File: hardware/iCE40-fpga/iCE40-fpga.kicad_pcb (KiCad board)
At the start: 4 copper layers, 50 x 22.9 mm, 66 parts, among them J1 USB_B_Micro, J2 JST_PH, J3 Feather, Q1 DMP2045U, U1 MCP73831-2-OT, U2 W25Q32JVZP, U3 AP2112K-3.3, U5 AP2112K-1.2, U6 ICE40UP5K-SG48ITR, U7 93C46B, U8 FT2232H, X1 DSC6101CI1A

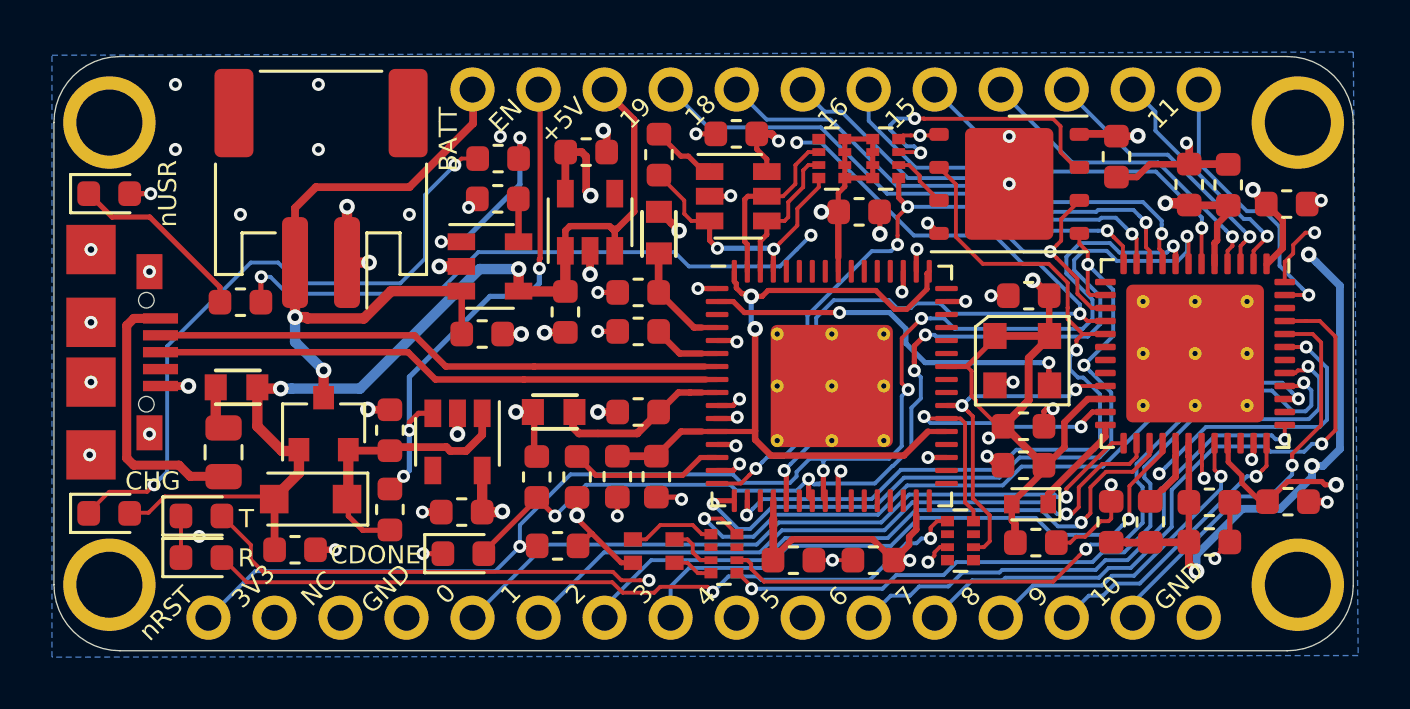
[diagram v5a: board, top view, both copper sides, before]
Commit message: changes to make everything work with new library setup
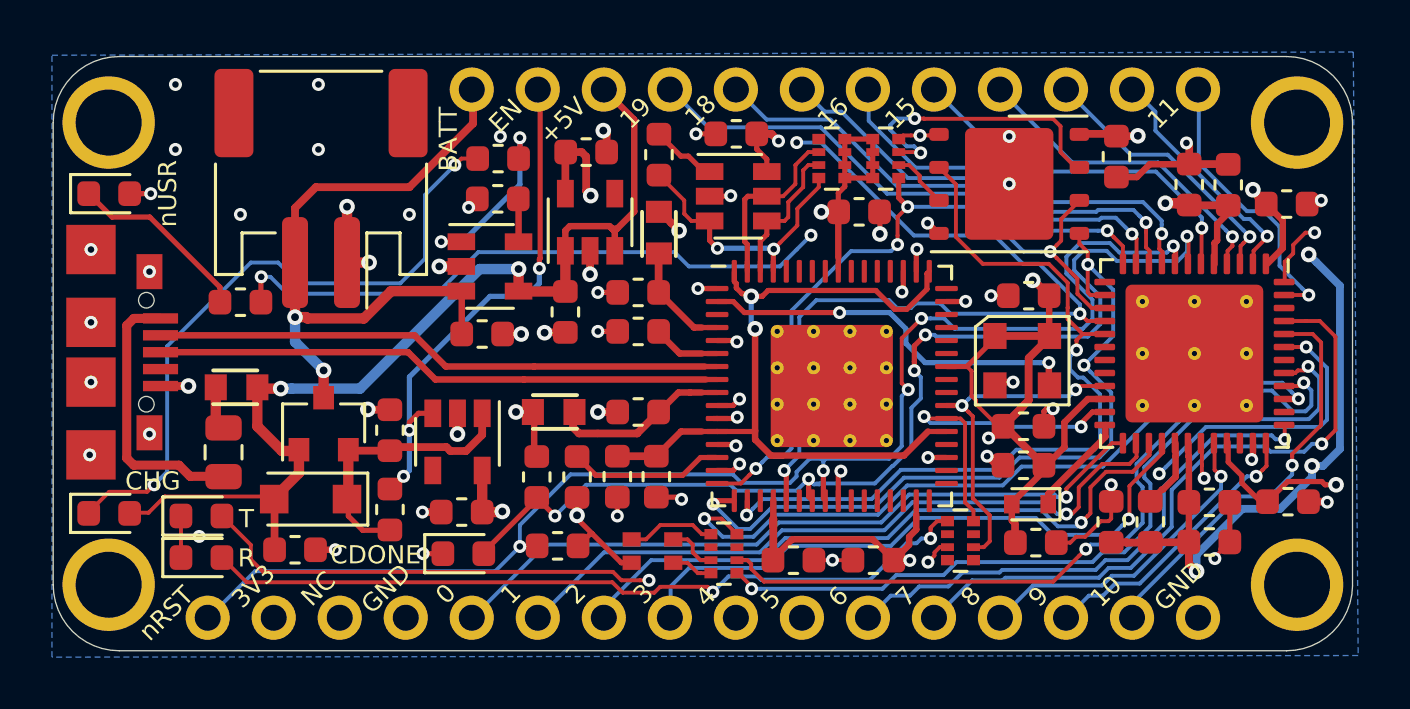
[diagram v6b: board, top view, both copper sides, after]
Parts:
- removed the REF** at (33.3, 38.6)
- removed the REF** at (66.7, 40.1)
- removed U8: FT2232H, josh-footprints:QFN-64-1EP_9x9mm_P0.5mm_EP4.7x4.7mm_ThermalVias
- added G***: LOGO, josh-logos:OSHW_Logo_3.6x3.6_F.Mask, B.Cu at (34.4, 39.0)
- added REF**: Josh Details, josh-logos:josh-details, B.Cu at (45.2, 39.5)
- added U4: ICE40UP5K-SG48ITR, josh-dfn-qfn:QFN-48-1EP_7x7mm_P0.5mm_EP5.3x5.3mm_ThermalVias, F.Cu at (70.2, 33.9)
- D6: value LTST-C19HE1WT -> LED_RGBA; footprint josh-footprints:0606LED -> josh-led:LED_0606
- F1: footprint josh-footprints:Fuse_0805_2012Metric -> josh-passives-smt:Fuse_0805_2012Metric
- FB1, FB2, FB3: value 600R -> 600R; footprint josh-footprints:BEADC1608X95N -> josh-passives-smt:Ferrite_Bead_0603
- J1: footprint josh-footprints:MicroUSB_Aliexpress -> josh-connectors:USB_Micro_Aliexpress
- J2: footprint josh-footprints:JST_PH_S2B-PH-SM4-TB_1x02-1MP_P2.00mm_Horizontal -> josh-connectors:JST_PH_S2B-PH-SM4-TB_1x02-1MP_P2.00mm_Horizontal
- J3: footprint josh-footprints:PCB_FeatherWing -> josh-connectors:featherwing
- U2: footprint josh-footprints:WSON-8-1EP_6x5mm_P1.27mm_EP3.4x4.3mm -> josh-soic-sot-etc:WSON-8-1EP_6x5mm_P1.27mm_EP3.4x4.3mm
- U6: value ICE40UP5K-SG48ITR -> 93C46B; footprint josh-footprints:QFN-48-1EP_7x7mm_P0.5mm_EP5.3x5.3mm_ThermalVias -> Package_TO_SOT_SMD:SOT-23-6
- U7: value 93C46B -> FT2232H; footprint Package_TO_SOT_SMD:SOT-23-6 -> josh-dfn-qfn:QFN-64-1EP_9x9mm_P0.5mm_EP4.7x4.7mm_ThermalVias
- X1: footprint josh-footprints:CDFN_3.2x2.5mm_XO -> josh-oscillators:CDFN_3.2x2.5mm_XO
- moved U6 18.6 mm to (52.6, 27.8), turned to 0 degrees
- moved U7 8.14 mm to (56.2, 35.1)
- turned FB1 to 0 degrees
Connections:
- FB1 pad 1: +5V -> Net-(F1-Pad1)
- FB1 pad 2: Net-(F1-Pad1) -> +5V
- U6 pad 1: +3V3 -> Net-(R13-Pad2)
- U6 pad 2: /IO12 -> GND
- U6 pad 3: /IO13 -> /FTDI Programmer / UART/FT_EEDATA
- U6 pad 4: /IO14 -> /FTDI Programmer / UART/FT_EECLK
- U6 pad 5: +1V2 -> /FTDI Programmer / UART/FT_EECS
- U6 pad 6: /IO15 -> +3V3
- U7 pad 1: Net-(R13-Pad2) -> GND
- U7 pad 2: GND -> /ICE_CLK
- U7 pad 3: /FTDI Programmer / UART/FT_EEDATA -> (no net)
- U7 pad 4: /FTDI Programmer / UART/FT_EECLK -> Net-(C32-Pad1)
- U7 pad 5: /FTDI Programmer / UART/FT_EECS -> GND
- U7 pad 6: +3V3 -> Net-(R15-Pad1)

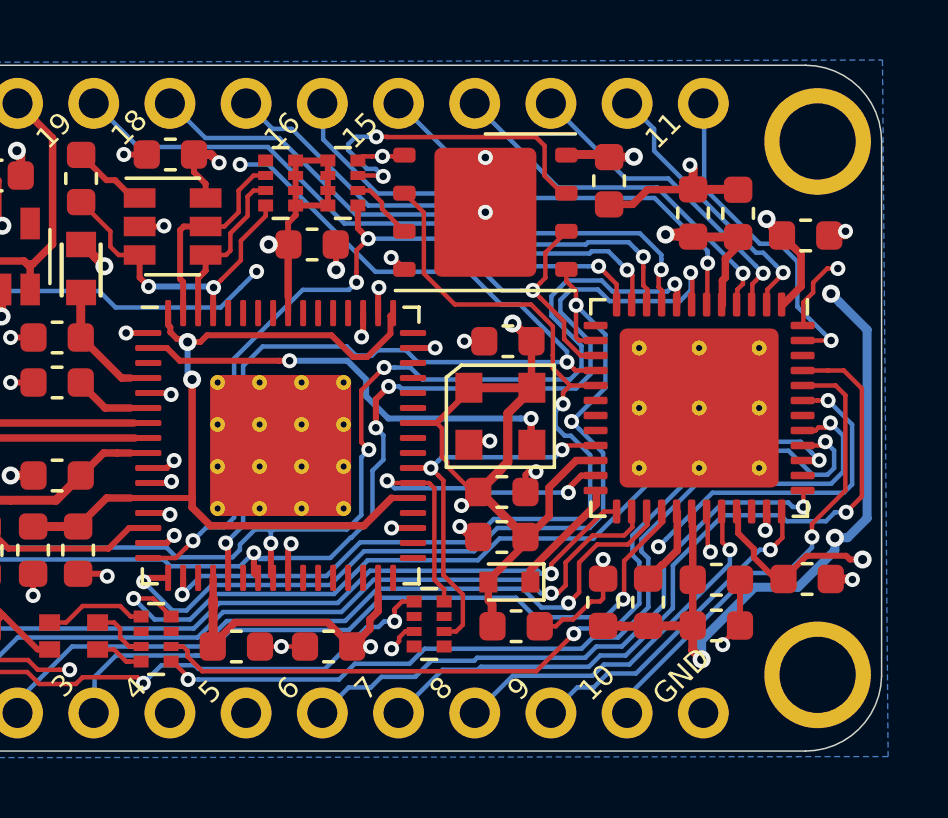
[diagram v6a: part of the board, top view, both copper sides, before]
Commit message: fixing things which broke resulting from library change
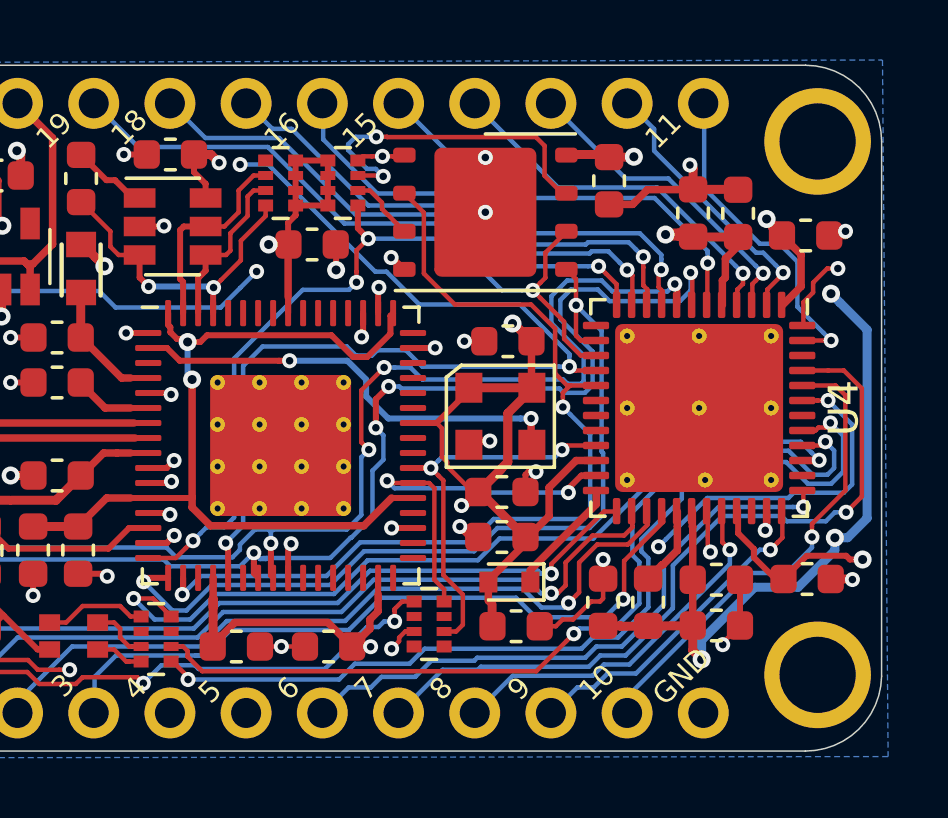
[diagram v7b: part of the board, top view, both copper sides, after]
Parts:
- U4: footprint josh-dfn-qfn:QFN-48-1EP_7x7mm_P0.5mm_EP5.3x5.3mm_ThermalVias -> josh-dfn-qfn:QFN-48-1EP_7x7mm_P0.5mm_EP5.6x5.6mm_ThermalVias
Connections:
- J1 pad 4: (no net) -> Net-(J1-Pad4)
- J3 pad 3: (no net) -> Net-(J3-Pad3)
- RN2 pad 1: (no net) -> Net-(RN2-Pad1)
- RN3 pad 3: (no net) -> Net-(RN3-Pad3)
- RN3 pad 6: (no net) -> Net-(RN3-Pad6)
- RN4 pad 2: (no net) -> Net-(RN4-Pad2)
- RN4 pad 4: (no net) -> Net-(RN4-Pad4)
- RN4 pad 5: (no net) -> Net-(RN4-Pad5)
- RN4 pad 7: (no net) -> Net-(RN4-Pad7)
- U3 pad 4: (no net) -> Net-(U3-Pad4)
- U4 pad 13: (no net) -> Net-(U4-Pad13)
- U4 pad 18: (no net) -> Net-(U4-Pad18)
- U4 pad 19: (no net) -> Net-(U4-Pad19)
- U4 pad 20: (no net) -> Net-(U4-Pad20)
- U4 pad 34: (no net) -> Net-(U4-Pad34)
- U4 pad 38: (no net) -> Net-(U4-Pad38)
- U4 pad 42: (no net) -> Net-(U4-Pad42)
- U4 pad 46: (no net) -> Net-(U4-Pad46)
- U5 pad 4: (no net) -> Net-(U5-Pad4)
- U7 pad 19: (no net) -> Net-(U7-Pad19)
- U7 pad 22: (no net) -> Net-(U7-Pad22)
- U7 pad 26: (no net) -> Net-(U7-Pad26)
- U7 pad 27: (no net) -> Net-(U7-Pad27)
- U7 pad 28: (no net) -> Net-(U7-Pad28)
- U7 pad 29: (no net) -> Net-(U7-Pad29)
- U7 pad 3: (no net) -> Net-(U7-Pad3)
- U7 pad 30: (no net) -> Net-(U7-Pad30)
- U7 pad 32: (no net) -> Net-(U7-Pad32)
- U7 pad 33: (no net) -> Net-(U7-Pad33)
- U7 pad 34: (no net) -> Net-(U7-Pad34)
- U7 pad 36: (no net) -> Net-(U7-Pad36)
- U7 pad 40: (no net) -> Net-(U7-Pad40)
- U7 pad 41: (no net) -> Net-(U7-Pad41)
- U7 pad 43: (no net) -> Net-(U7-Pad43)
- U7 pad 44: (no net) -> Net-(U7-Pad44)
- U7 pad 45: (no net) -> Net-(U7-Pad45)
- U7 pad 46: (no net) -> Net-(U7-Pad46)
- U7 pad 48: (no net) -> Net-(U7-Pad48)
- U7 pad 52: (no net) -> Net-(U7-Pad52)
- U7 pad 53: (no net) -> Net-(U7-Pad53)
- U7 pad 54: (no net) -> Net-(U7-Pad54)
- U7 pad 55: (no net) -> Net-(U7-Pad55)
- U7 pad 57: (no net) -> Net-(U7-Pad57)
- U7 pad 58: (no net) -> Net-(U7-Pad58)
- U7 pad 59: (no net) -> Net-(U7-Pad59)
- U7 pad 60: (no net) -> Net-(U7-Pad60)
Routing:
- net /nLED_RED: track 30.0 -> 31.0 mm
- net /FLASH_MOSI|IO0: track 29.3 -> 28.4 mm, vias 3 -> 2
- net /ICE_SS: track 40.2 -> 40.7 mm

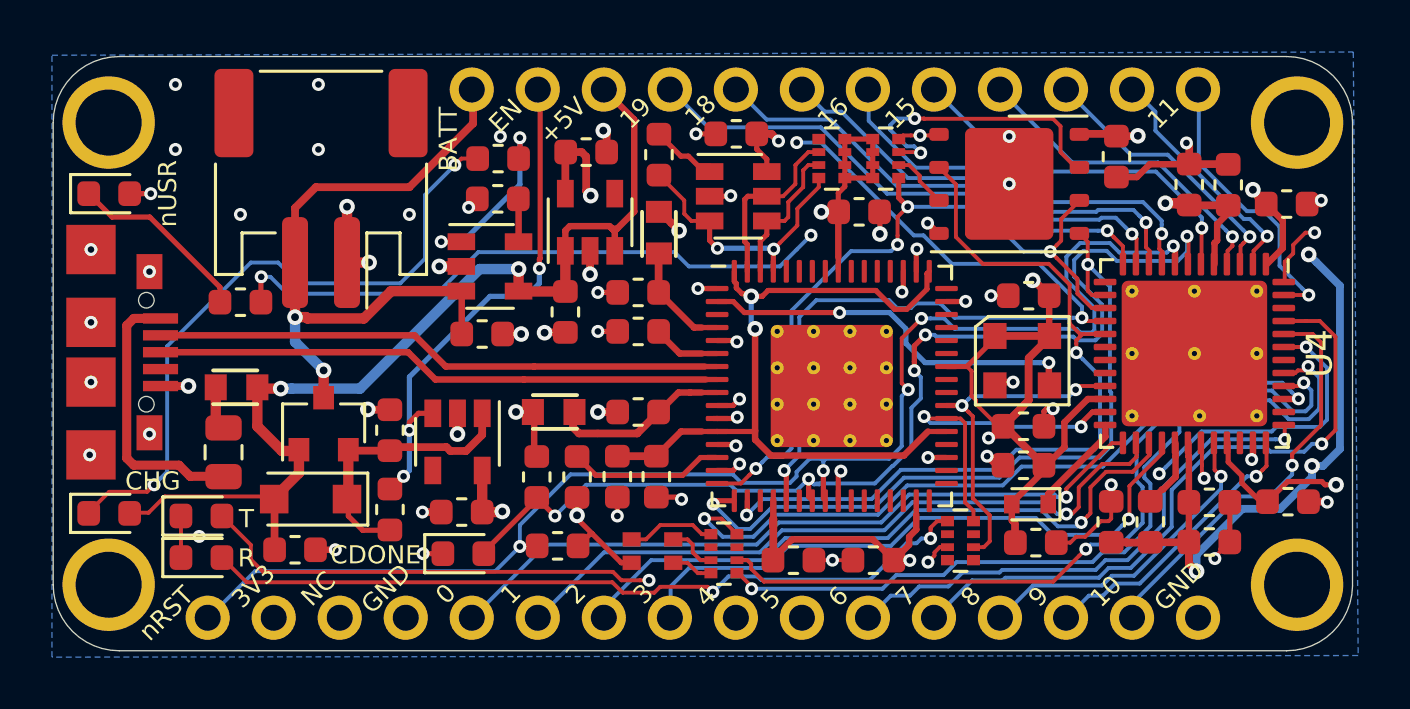
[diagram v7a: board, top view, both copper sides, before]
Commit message: added multiplexing featherwing
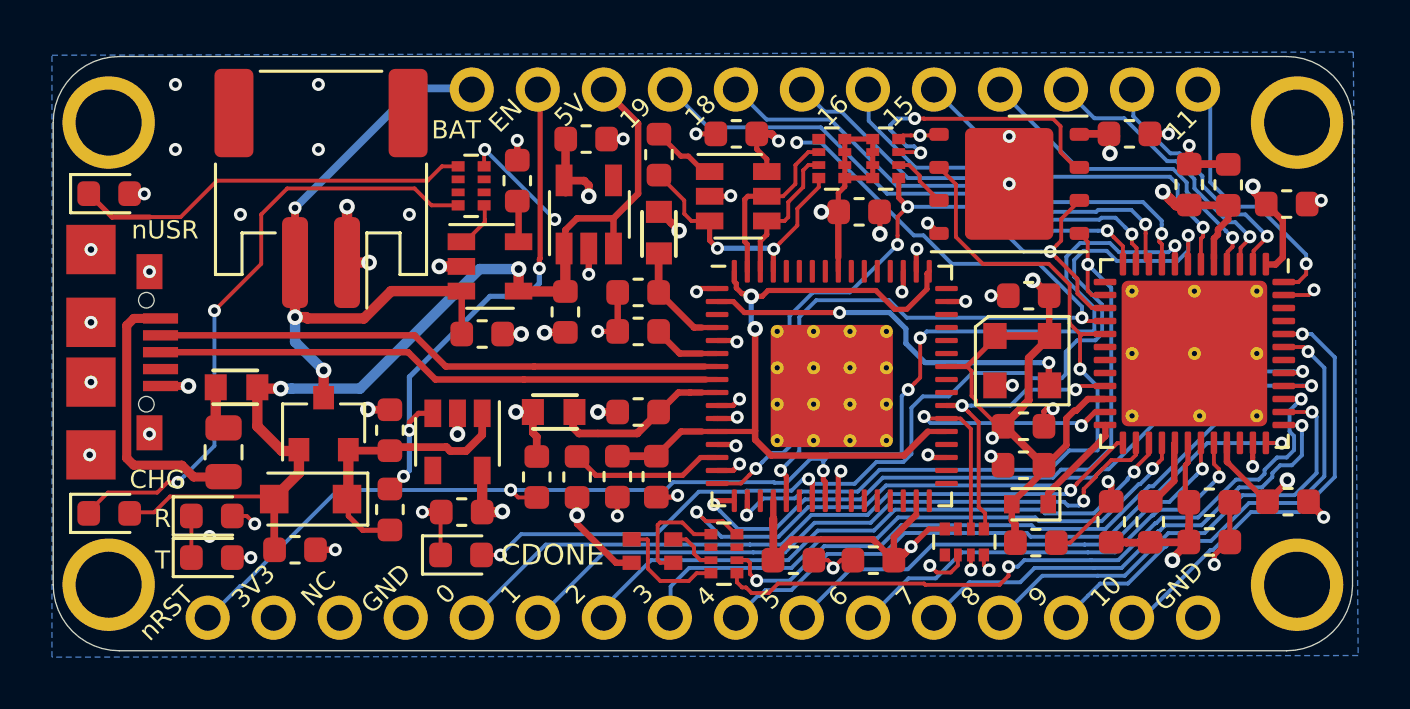
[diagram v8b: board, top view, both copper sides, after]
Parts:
- removed R2, R7: 2K2, Resistor_SMD:R_0603_1608Metric
- removed R8: 1K, Resistor_SMD:R_0603_1608Metric
- added RN5: 2K2, Resistor_SMD:R_Array_Convex_4x0402, F.Cu at (42.4, 27.4)
- RN4: value 330R -> 2K2
- U5: value AP2112K-1.2 -> NCV8114ASN120T1G; footprint Package_TO_SOT_SMD:SOT-23-5 -> Package_TO_SOT_SMD:TSOT-23-5
- moved R5 2.77 mm to (44.9, 38.6), turned to 270 degrees
- moved R3 1.03 mm to (44.1, 27.2), turned to 90 degrees
- moved C7 1.01 mm to (67.7, 25.4), turned to 0 degrees
- moved G*** 0.82 mm to (34.9, 38.4)
- moved C6 0.50 mm to (46.8, 25.6)
- moved D3 0.40 mm to (32.4, 41.7)
- moved D8 0.40 mm to (32.4, 40.1)
- moved U5 0.30 mm to (46.9, 28.5)
- moved RN4 0.16 mm to (61.4, 41.1), turned to 90 degrees
- moved D5 0.10 mm to (42.0, 41.6)
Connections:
- RN3 pad 1: /nLED_RED -> /nLED_BLUE
- RN3 pad 4: /nLED_BLUE -> /nLED_RED
- RN3 pad 5: Net-(D6-Pad3) -> Net-(D6-Pad1)
- RN3 pad 8: Net-(D6-Pad1) -> Net-(D6-Pad3)
- RN4 pad 1: Net-(D3-Pad2) -> Net-(RN4-Pad1)
- RN4 pad 2: Net-(RN4-Pad2) -> /ICE_CDONE
- RN4 pad 4: Net-(RN4-Pad4) -> Net-(D3-Pad2)
- RN4 pad 5: Net-(RN4-Pad5) -> /TX_FPGA
- RN4 pad 6: /TX_FPGA -> /RX_FPGA
- RN4 pad 7: Net-(RN4-Pad7) -> +3V3
- RN4 pad 8: /RX_FPGA -> +3V3
- U4 pad 32: /IO8 -> /IO6
- U4 pad 36: /IO9 -> /IO4
- U4 pad 37: /IO6 -> /IO7
- U4 pad 38: Net-(U4-Pad38) -> /IO8
- U4 pad 43: /IO4 -> /IO9
- U4 pad 45: /IO7 -> Net-(U4-Pad45)
- U4 pad 47: /IO11 -> /nLED
- U4 pad 48: /nLED -> /IO11
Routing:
- net /nLED: track 48.1 -> 39.6 mm
- net Net-(D7-Pad1): track 7.12 -> 15.4 mm
- net /IO9: track 11.3 -> 18.6 mm
- net /IO4: track 31.8 -> 24.5 mm, vias 2 -> 1
- net /IO7: track 25.2 -> 18.7 mm
- net /ICE_CDONE: track 41.8 -> 47.7 mm, vias 5 -> 4
- net /IO8: track 12.4 -> 18.0 mm
- net Net-(RN5-Pad1): track 7.33 -> 1.97 mm, vias 2 -> 0
- net /IO6: track 20.2 -> 17.2 mm
- net /nLED_GREEN: track 29.9 -> 27.0 mm
- net Net-(D6-Pad1): track 1.62 -> 4.27 mm
- net +1V2: track 64.2 -> 66.4 mm, vias 5 -> 3
- net /nLED_RED: track 31.0 -> 29.0 mm
- net Net-(D1-Pad1): track 25.6 -> 23.9 mm
- net /IO5: track 20.1 -> 18.8 mm
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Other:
- board text added: "5V"
- board text added: "BAT"
- board text removed: "+5V"
- board text removed: "BATT"
